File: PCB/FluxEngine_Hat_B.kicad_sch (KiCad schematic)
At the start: 4 parts, among them J1 CY8CKIT-059, P1 FDD_IBMPC_host, P2 FDD_SA800_host

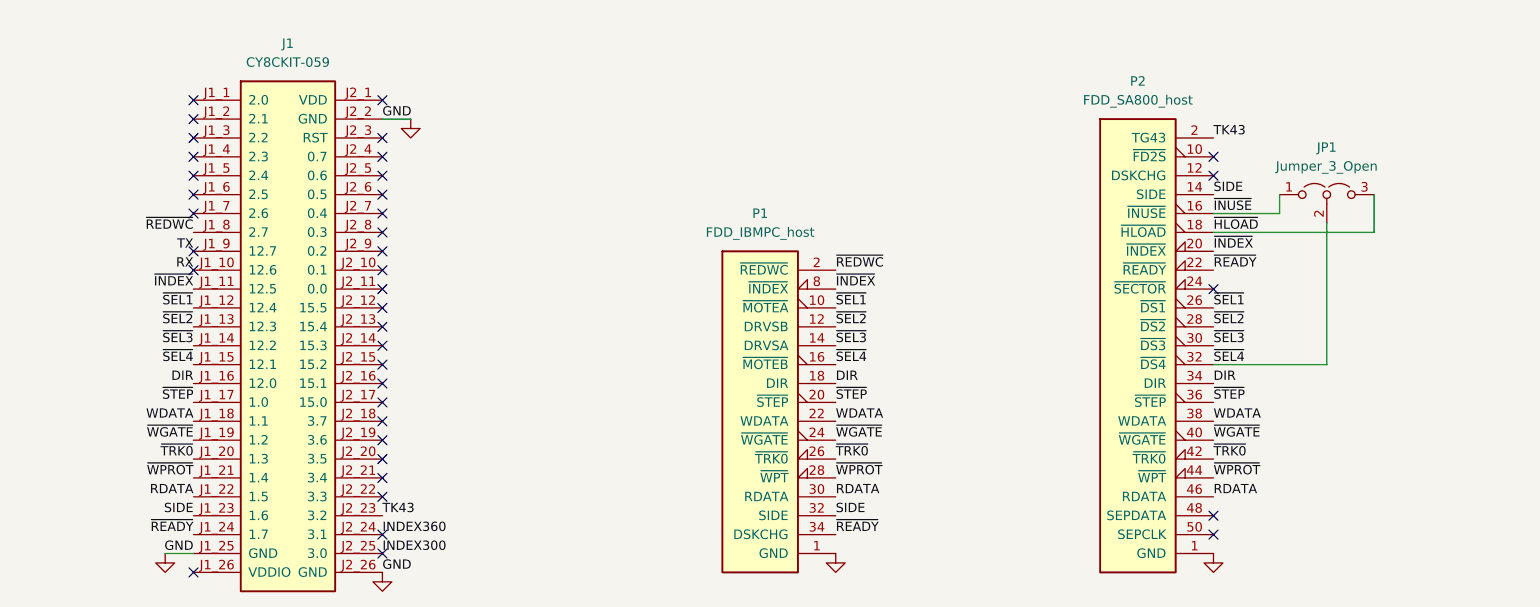
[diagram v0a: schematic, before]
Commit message: snap cover, better 3d model files
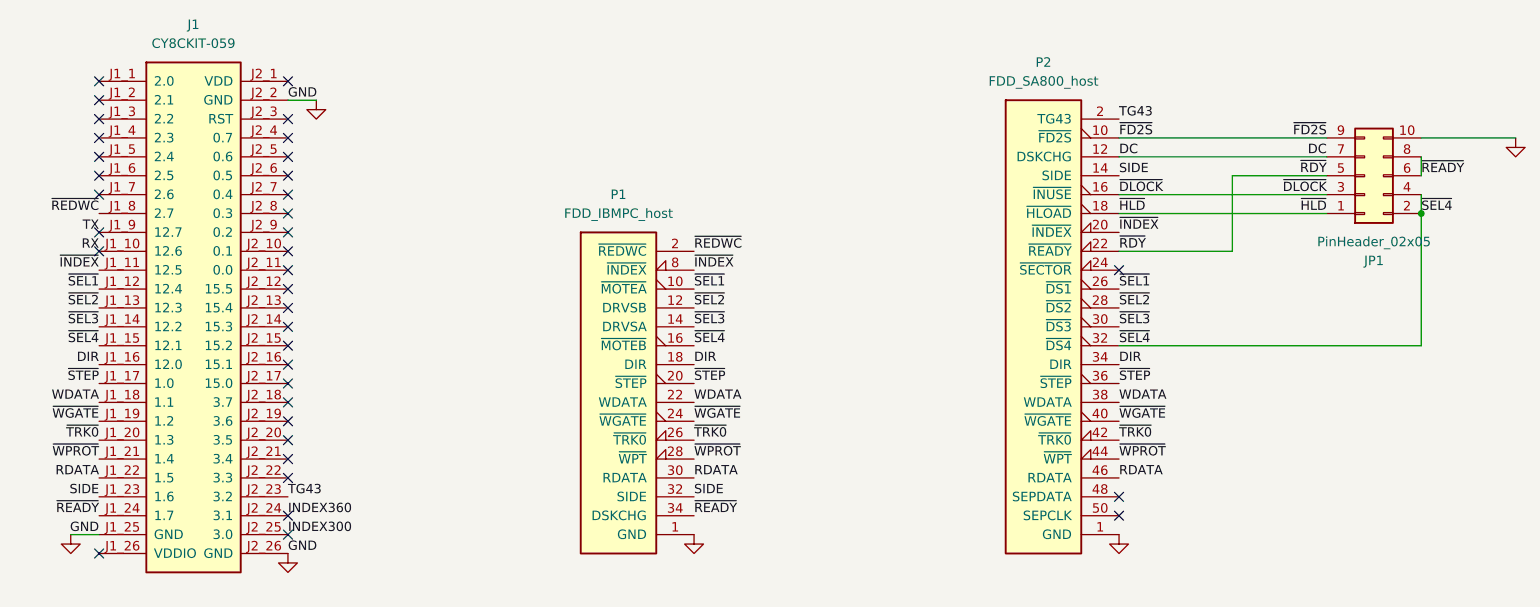
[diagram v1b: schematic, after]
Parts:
- removed JP1: Jumper_3_Open, 000_LOCAL:PinHeader_1x03_P2.54mm_Vertical bare, symbol 000_LOCAL:Jumper_3_Open
- added JP1: PinHeader_02x05, 000_LOCAL:PinHeader_2x05_P2.54mm_Vertical, symbol 000_LOCAL:Conn_02x05_Odd_Even
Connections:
- net GND: now also JP1.10 (Pin_10)
- net ~{READY}: now also JP1.6 (Pin_6), JP1.8 (Pin_8); no longer P2.22 (~{READY})
- net ~{SEL4}: now also JP1.2 (Pin_2), JP1.4 (Pin_4)
- net ~{FD2S}: now reaches P2.10 (~{FD2S})
- net ~{FD2S}: now also JP1.9 (Pin_9)
- net DC: now reaches P2.12 (DSKCHG)
- net DC: now also JP1.7 (Pin_7)
- net TK43 renamed TG43
- net ~{HLOAD} renamed ~{HLD}
- net ~{HLD}: now also JP1.1 (Pin_1)
- net ~{INUSE} renamed ~{DLOCK}
- net ~{DLOCK}: now also JP1.3 (Pin_3)
- new net ~{RDY}: JP1.5 (Pin_5), P2.22 (~{READY})
- no-connect marks 38 -> 36
